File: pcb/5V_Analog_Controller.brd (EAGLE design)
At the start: 50 x 36 mm, 24 parts, among them J1 POWER, Q1 AO3400, Q2 AO3400, U1 ESP32-PICO-MINI-02, U2 AP2112K, X1 PROG, X2 SS-52100-001, X3 SS-52100-001, X5 BOOT, X6 RESET

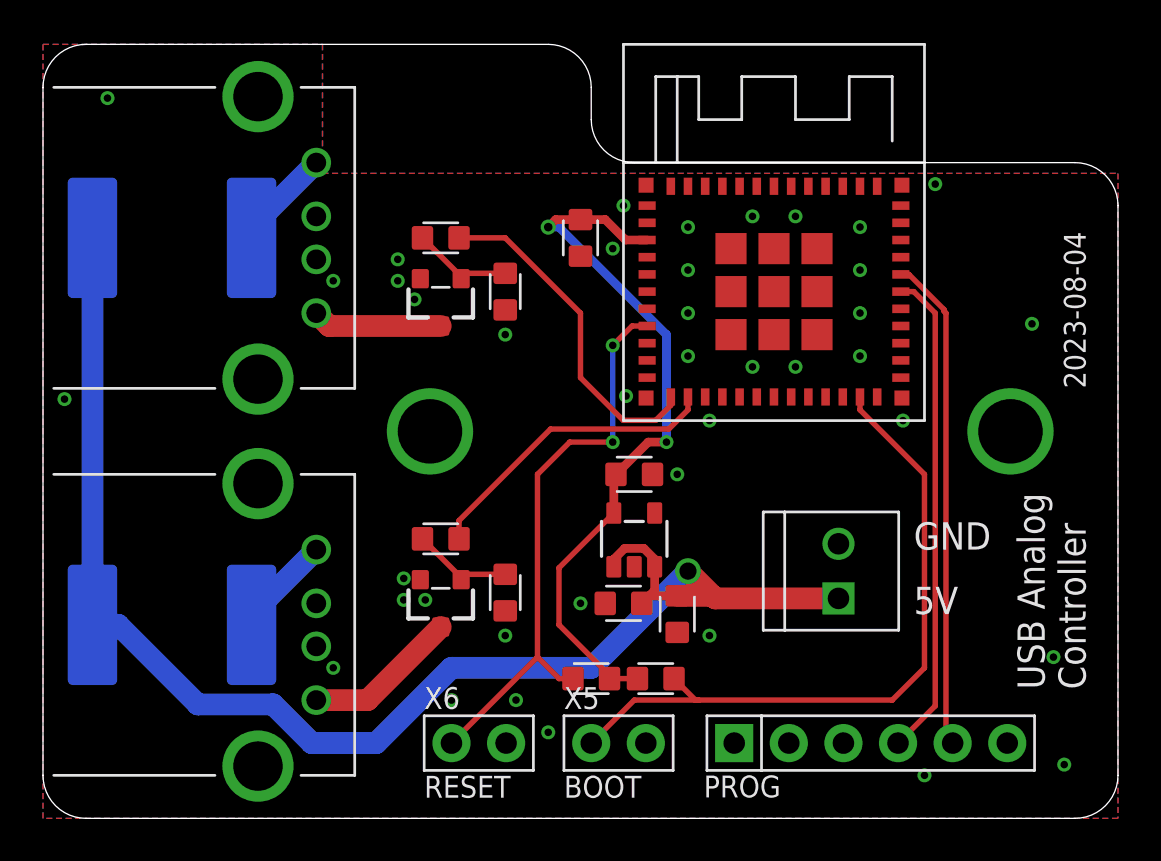
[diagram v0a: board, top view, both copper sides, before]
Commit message: Switch to input power jack
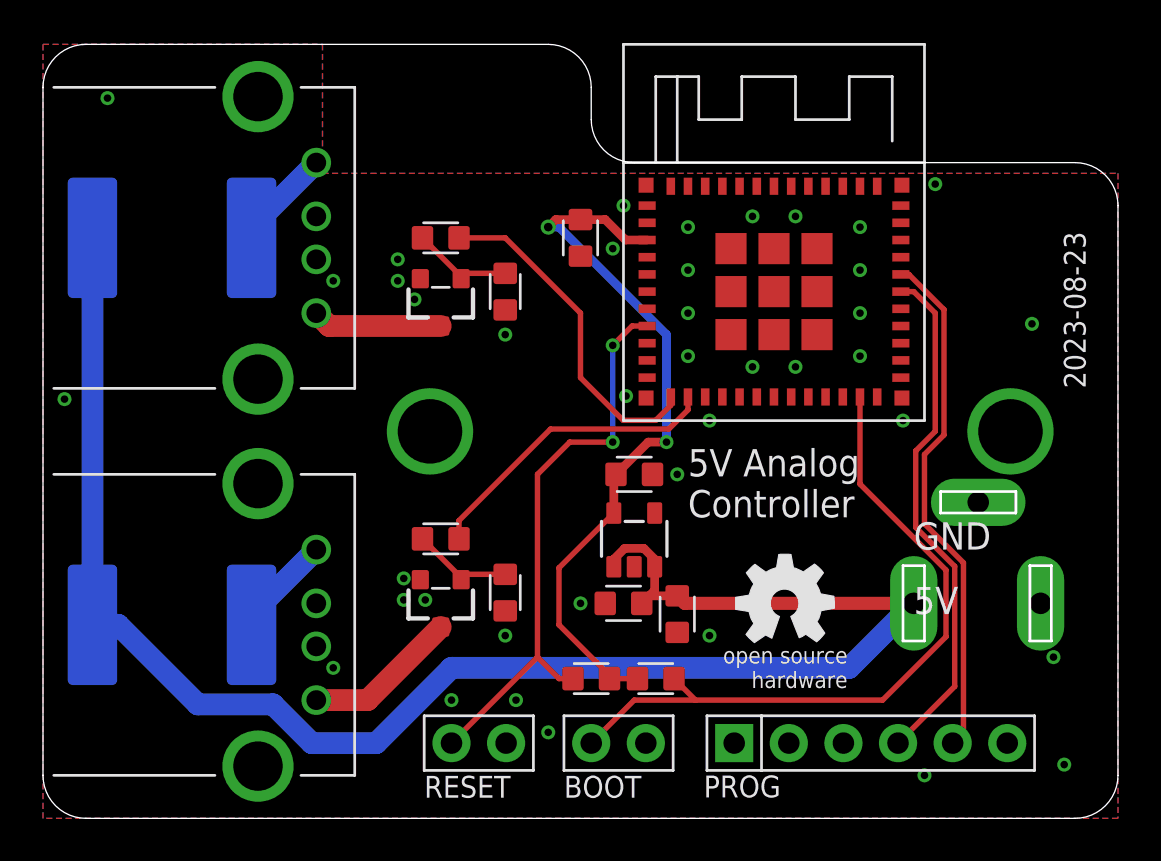
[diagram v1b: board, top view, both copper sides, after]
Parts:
- added U$3: (no value), M2M-Frames:OSHW-5MM-TPLACE
- J1: device M2M-Connectors:TERMINAL-2.54-2P -> M2M-Connectors:XKB-DC-005-5A-2.0
- moved J1 6.67 mm to (43.5, 10.0), turned to 180 degrees
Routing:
- net VIN: track 67.2 -> 79.1 mm, vias 1 -> 0
- net RXD0: track 22.7 -> 24.2 mm
- net TXD0: track 23.0 -> 24.2 mm
- net IO0: track 32.2 -> 32.8 mm
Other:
- board text added: "2023-08-23"
- board text added: "5V Analog Controller"
- board text removed: "2023-08-04"
- board text removed: "USB Analog Controller"
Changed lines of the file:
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@@
 <drawing>
 <settings>
-<setting alwaysvectorfont="no"/>
+<setting alwaysvectorfont="yes"/>
 <setting verticaltext="up"/>
 </settings>
@@
 <wire x1="23.5" y1="36" x2="2" y2="36" width="0" layer="20"/>
 <wire x1="2" y1="36" x2="0" y2="34" width="0" layer="20" curve="90"/>
-<text x="48.5" y="6" size="1.27" layer="21" rot="R90">USB Analog
+<text x="30" y="14" size="1.27" layer="21">5V Analog
 Controller</text>
-<text x="48.5" y="20" size="1.016" layer="21" rot="R90">2023-08-04</text>
+<text x="48.5" y="20" size="1.016" layer="21" rot="R90">2023-08-23</text>
 <text x="40.5" y="12.5" size="1.27" layer="21">GND</text>
 <text x="40.5" y="9.5" size="1.27" layer="21">5V</text>
@@
 <dimension x1="18" y1="18" x2="18" y2="0" x3="-6" y3="9" textsize="1.778" layer="47"/>
 <dimension x1="0" y1="0" x2="0" y2="36" x3="-13" y3="18" textsize="1.778" layer="47"/>
-<text x="54.5" y="20" size="1.778" layer="47">Mounting holes
+<text x="42.5" y="31.5" size="1.778" layer="47">Mounting holes
 2x3mm</text>
 <dimension x1="10" y1="9" x2="10" y2="0" x3="-2.5" y3="4.5" textsize="1.778" layer="47"/>
 <dimension x1="10" y1="27" x2="10" y2="0" x3="-9.5" y3="13.5" textsize="1.778" layer="47"/>
-<dimension x1="48" y1="30.5" x2="48" y2="0" x3="53.5" y3="15.25" textsize="1.778" layer="47"/>
+<dimension x1="48" y1="30.5" x2="48" y2="0" x3="63" y3="15.25" textsize="1.778" layer="47"/>
 <dimension x1="0" y1="34" x2="25.5" y2="34" x3="12.75" y3="38.5" textsize="1.778" layer="47"/>
+<dimension x1="43.5" y1="10" x2="43.5" y2="0" x3="59.5" y3="5" textsize="1.778" layer="47"/>
 </plain>
 <attributes>
@@
 </element>
 <element name="X5" library="M2M-Connectors" package="1X02-2.54" value="BOOT" x="25.5" y="3.5" smashed="yes">
-<attribute name="NAME" x="24.865" y="2.865" size="0.8128" layer="51"/>
 <attribute name="NAME" x="24.23" y="5.0875" size="1.016" layer="25"/>
 <attribute name="NAME" x="24.611" y="2.865" size="1.27" layer="48"/>
+<attribute name="NAME" x="24.865" y="2.865" size="0.8128" layer="51"/>
 <attribute name="VALUE" x="24.23" y="0.96" size="1.016" layer="21"/>
 </element>
 <element name="X6" library="M2M-Connectors" package="1X02-2.54" value="RESET" x="19" y="3.5" smashed="yes">
-<attribute name="NAME" x="18.865" y="2.365" size="0.8128" layer="51"/>
 <attribute name="NAME" x="17.73" y="5.0875" size="1.016" layer="25"/>
 <attribute name="NAME" x="18.111" y="2.865" size="1.27" layer="48"/>
+<attribute name="NAME" x="18.865" y="2.365" size="0.8128" layer="51"/>
 <attribute name="VALUE" x="17.73" y="0.96" size="1.016" layer="21"/>
 </element>
-<element name="J1" library="M2M-Connectors" package="TERMINAL-2.54-2P" value="POWER" x="37" y="11.5" smashed="yes" rot="R90"/>
+<element name="J1" library="M2M-Connectors" package="XKB-DC-005-5A-2.0" value="POWER" x="43.5" y="10" smashed="yes" rot="R180"/>
 <element name="U2" library="M2M-IC" package="SOT23-5" value="AP2112K" x="27.5" y="13" smashed="yes">
 <attribute name="NAME" x="27.495" y="14.805" size="1.016" layer="25" align="bottom-center"/>
@@
 <attribute name="VALUE" x="1" y="13.5" size="1.016" layer="28" rot="MR180"/>
 </element>
+<element name="U$3" library="M2M-Frames" package="OSHW-5MM-TPLACE" value="" x="34.5" y="10" smashed="yes"/>
 </elements>
 <signals>
@@
 <wire x1="26.5" y1="6.5" x2="27.65" y2="6.5" width="0.254" layer="1"/>
 <wire x1="26.55" y1="14.2" x2="24" y2="11.65" width="0.254" layer="1"/>
-<wire x1="24" y1="9" x2="26.5" y2="6.5" width="0.254" layer="1"/>
+<wire x1="24" y1="9" x2="25.75" y2="7.25" width="0.254" layer="1"/>
+<wire x1="25.75" y1="7.25" x2="26.5" y2="6.5" width="0.254" layer="1"/>
 <wire x1="24" y1="11.65" x2="24" y2="9" width="0.254" layer="1"/>
 </signal>
@@
 <contactref element="U1" pad="23"/>
 <contactref element="X5" pad="1"/>
-<wire x1="38" y1="19" x2="38" y2="19.6" width="0.254" layer="1"/>
 <wire x1="25.5" y1="3.5" x2="27.5" y2="5.5" width="0.254" layer="1"/>
-<wire x1="39.5" y1="5.5" x2="41" y2="7" width="0.254" layer="1"/>
-<wire x1="41" y1="7" x2="41" y2="16" width="0.254" layer="1"/>
-<wire x1="41" y1="16" x2="38" y2="19" width="0.254" layer="1"/>
 <wire x1="27.5" y1="5.5" x2="30.35" y2="5.5" width="0.254" layer="1"/>
 <contactref element="R5" pad="1"/>
-<wire x1="30.5" y1="5.5" x2="39.5" y2="5.5" width="0.254" layer="1"/>
 <wire x1="29.35" y1="6.5" x2="30.35" y2="5.5" width="0.254" layer="1"/>
-<wire x1="30.35" y1="5.5" x2="30.5" y2="5.5" width="0.254" layer="1"/>
+<wire x1="30.35" y1="5.5" x2="39.05076875" y2="5.5" width="0.254" layer="1"/>
+<wire x1="39.05076875" y1="5.5" x2="42" y2="8.44923125" width="0.254" layer="1"/>
+<wire x1="42" y1="8.44923125" x2="42" y2="11.55076875" width="0.254" layer="1"/>
+<wire x1="42" y1="11.55076875" x2="38" y2="15.55076875" width="0.254" layer="1"/>
+<wire x1="38" y1="15.55076875" x2="38" y2="19.6" width="0.254" layer="1"/>
 </signal>
 <signal name="EN">
@@
 <contactref element="U1" pad="31"/>
 <contactref element="X1" pad="RX"/>
-<wire x1="41.9064" y1="23.6683375" x2="41.9064" y2="23.5936" width="0.254" layer="1"/>
-<wire x1="41.9064" y1="23.5936" x2="42" y2="23.5" width="0.254" layer="1"/>
-<wire x1="39.9" y1="25.3" x2="40.2747375" y2="25.3" width="0.254" layer="1"/>
-<wire x1="40.2747375" y1="25.3" x2="41.9064" y2="23.6683375" width="0.254" layer="1"/>
-<wire x1="42" y1="3.81" x2="42.31" y2="3.5" width="0.254" layer="1"/>
-<wire x1="42" y1="23.5" x2="42" y2="3.81" width="0.254" layer="1"/>
+<wire x1="39.9" y1="25.3" x2="40" y2="25.3" width="0.254" layer="1"/>
+<wire x1="42.31" y1="3.5" x2="42.8128" y2="4.0028" width="0.254" layer="1"/>
+<wire x1="42.8128" y1="4.0028" x2="42.8128" y2="11.88744375" width="0.254" layer="1"/>
+<wire x1="42.8128" y1="11.88744375" x2="41" y2="13.70024375" width="0.254" layer="1"/>
+<wire x1="41.9064" y1="17.8316625" x2="41.9064" y2="23.6683375" width="0.254" layer="1"/>
+<wire x1="40.2747375" y1="25.3" x2="40" y2="25.3" width="0.254" layer="1"/>
+<wire x1="41" y1="13.70024375" x2="41" y2="16.9252625" width="0.254" layer="1"/>
+<wire x1="41" y1="16.9252625" x2="41.9064" y2="17.8316625" width="0.254" layer="1"/>
+<wire x1="41.9064" y1="23.6683375" x2="40.2747375" y2="25.3" width="0.254" layer="1"/>
 </signal>
 <signal name="RXD0">
 <contactref element="U1" pad="30"/>
 <contactref element="X1" pad="TX"/>
+<wire x1="39.77" y1="3.5" x2="42.4064" y2="6.1364" width="0.254" layer="1"/>
+<wire x1="42.4064" y1="11.71910625" x2="42.4064" y2="6.1364" width="0.254" layer="1"/>
 <wire x1="39.9" y1="24.5" x2="40.5" y2="24.5" width="0.254" layer="1"/>
-<wire x1="41.5" y1="5.23" x2="39.77" y2="3.5" width="0.254" layer="1"/>
+<wire x1="41.5" y1="23.5" x2="41.5" y2="18" width="0.254" layer="1"/>
 <wire x1="40.5" y1="24.5" x2="41.5" y2="23.5" width="0.254" layer="1"/>
-<wire x1="41.5" y1="23.5" x2="41.5" y2="5.23" width="0.254" layer="1"/>
+<wire x1="41.5" y1="18" x2="40.5936" y2="17.0936" width="0.254" layer="1"/>
+<wire x1="40.5936" y1="17.0936" x2="40.5936" y2="13.53190625" width="0.254" layer="1"/>
+<wire x1="40.5936" y1="13.53190625" x2="42.4064" y2="11.71910625" width="0.254" layer="1"/>
 </signal>
 <signal name="N$1">
@@
 <contactref element="U2" pad="3"/>
 <contactref element="C2" pad="1"/>
-<via x="30" y="11.5" extent="1-16" drill="0.8"/>
 <wire x1="28.45" y1="11.7" x2="28.45" y2="10.6" width="0.4064" layer="1"/>
 <wire x1="28.45" y1="10.6" x2="27.85" y2="10" width="0.4064" layer="1"/>
@@
 <wire x1="28.2" y1="10.35" x2="29.5" y2="10.35" width="0.4064" layer="1"/>
 <wire x1="12.5" y1="3.5" x2="15.5" y2="3.5" width="1.016" layer="16"/>
-<wire x1="25.5" y1="7" x2="30" y2="11.5" width="1.016" layer="16"/>
 <wire x1="15.5" y1="3.5" x2="19" y2="7" width="1.016" layer="16"/>
-<wire x1="19" y1="7" x2="25.5" y2="7" width="1.016" layer="16"/>
 <wire x1="26.55" y1="11.7" x2="26.55" y2="12.0516375" width="0.4064" layer="1"/>
 <wire x1="27.0539625" y1="12.5556" x2="26.55" y2="12.0516375" width="0.4064" layer="1"/>
@@
 <wire x1="7.2" y1="5.3" x2="10.7" y2="5.3" width="1.016" layer="16"/>
 <wire x1="3.5" y1="9" x2="7.2" y2="5.3" width="1.016" layer="16"/>
-<wire x1="37" y1="10.23" x2="31.27" y2="10.23" width="1.016" layer="1"/>
-<wire x1="31.15" y1="10.35" x2="30" y2="11.5" width="1.016" layer="1"/>
-<wire x1="29.5" y1="10.35" x2="31.15" y2="10.35" width="1.016" layer="1"/>
-<wire x1="31.15" y1="10.35" x2="31.27" y2="10.23" width="1.016" layer="1"/>
+<wire x1="37.5" y1="7" x2="40.5" y2="10" width="1.016" layer="16"/>
+<wire x1="19" y1="7" x2="37.5" y2="7" width="1.016" layer="16"/>
+<wire x1="40.5" y1="10" x2="29.85" y2="10" width="0.6096" layer="1"/>
+<wire x1="29.85" y1="10" x2="29.5" y2="10.35" width="0.6096" layer="1"/>
 </signal>
 <signal name="N$5">

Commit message: Add reverse power protection for internal circuits
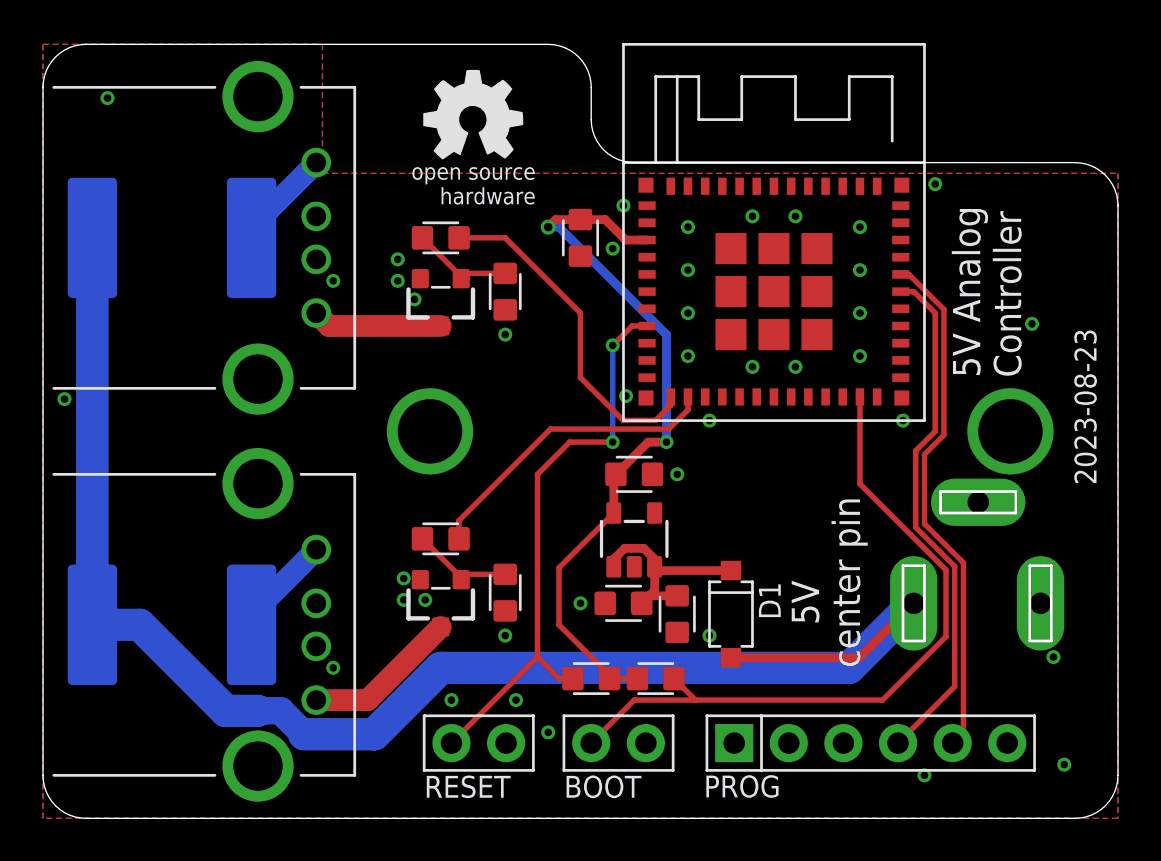
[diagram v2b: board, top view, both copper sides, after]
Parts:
- added D1: B5819LW, M2M-DiscreteSemi:SOD-123
- moved U$3 26.8 mm to (20.0, 32.5)
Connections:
- new net VSW: D1.A, F1.A, F2.A, J1.1
- net VIN: now also D1.C; no longer F1.A, F2.A, J1.1
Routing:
- net VSW: track 0.00 -> 70.4 mm
- net VIN: track 79.1 -> 10.4 mm
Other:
- board text added: "5V center pin"
- board text removed: "5V"
- board text removed: "GND"
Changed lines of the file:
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@@
 <wire x1="23.5" y1="36" x2="2" y2="36" width="0" layer="20"/>
 <wire x1="2" y1="36" x2="0" y2="34" width="0" layer="20" curve="90"/>
-<text x="30" y="14" size="1.27" layer="21">5V Analog
+<text x="45.5" y="20.5" size="1.27" layer="21" rot="R90">5V Analog
 Controller</text>
-<text x="48.5" y="20" size="1.016" layer="21" rot="R90">2023-08-23</text>
-<text x="40.5" y="12.5" size="1.27" layer="21">GND</text>
-<text x="40.5" y="9.5" size="1.27" layer="21">5V</text>
+<text x="49" y="15.5" size="1.016" layer="21" rot="R90">2023-08-23</text>
+<text x="38" y="7" size="1.27" layer="21" rot="R90">    5V
+center pin</text>
 <dimension x1="18" y1="18" x2="0" y2="18" x3="9" y3="-4.5" textsize="1.778" layer="47"/>
 <dimension x1="45" y1="18" x2="0" y2="18" x3="22.5" y3="-8.5" textsize="1.778" layer="47"/>
@@
 <attribute name="VALUE" x="1" y="13.5" size="1.016" layer="28" rot="MR180"/>
 </element>
-<element name="U$3" library="M2M-Frames" package="OSHW-5MM-TPLACE" value="" x="34.5" y="10" smashed="yes"/>
+<element name="U$3" library="M2M-Frames" package="OSHW-5MM-TPLACE" value="" x="20" y="32.5" smashed="yes"/>
+<element name="D1" library="M2M-DiscreteSemi" package="SOD-123" value="B5819LW" x="32" y="9.5" smashed="yes" rot="R270">
+<attribute name="NAME" x="32" y="9.5" size="0.8128" layer="51" rot="R270" align="center"/>
+<attribute name="NAME" x="33.3" y="11" size="1.016" layer="21" rot="R270"/>
+<attribute name="VALUE" x="29.7" y="11" size="1.016" layer="27" rot="R270"/>
+</element>
 </elements>
 <signals>
@@
 <signal name="VIN">
 <contactref element="U2" pad="1"/>
-<contactref element="J1" pad="1"/>
 <contactref element="C3" pad="1"/>
 <contactref element="U2" pad="3"/>
@@
 <wire x1="27.85" y1="10" x2="28.2" y2="10.35" width="0.4064" layer="1"/>
 <wire x1="28.2" y1="10.35" x2="29.5" y2="10.35" width="0.4064" layer="1"/>
-<wire x1="12.5" y1="3.5" x2="15.5" y2="3.5" width="1.016" layer="16"/>
-<wire x1="15.5" y1="3.5" x2="19" y2="7" width="1.016" layer="16"/>
 <wire x1="26.55" y1="11.7" x2="26.55" y2="12.0516375" width="0.4064" layer="1"/>
 <wire x1="27.0539625" y1="12.5556" x2="26.55" y2="12.0516375" width="0.4064" layer="1"/>
@@
 <wire x1="28.45" y1="12.0516375" x2="27.9460375" y2="12.5556" width="0.4064" layer="1"/>
 <wire x1="27.9460375" y1="12.5556" x2="27.0539625" y2="12.5556" width="0.4064" layer="1"/>
-<contactref element="F1" pad="A"/>
-<contactref element="F2" pad="A"/>
-<wire x1="10.7" y1="5.3" x2="12.5" y2="3.5" width="1.016" layer="16"/>
-<wire x1="2.3" y1="27" x2="2.3" y2="9" width="1.016" layer="16"/>
-<wire x1="2.3" y1="9" x2="3.5" y2="9" width="1.016" layer="16"/>
-<wire x1="7.2" y1="5.3" x2="10.7" y2="5.3" width="1.016" layer="16"/>
-<wire x1="3.5" y1="9" x2="7.2" y2="5.3" width="1.016" layer="16"/>
-<wire x1="37.5" y1="7" x2="40.5" y2="10" width="1.016" layer="16"/>
-<wire x1="19" y1="7" x2="37.5" y2="7" width="1.016" layer="16"/>
-<wire x1="40.5" y1="10" x2="29.85" y2="10" width="0.6096" layer="1"/>
-<wire x1="29.85" y1="10" x2="29.5" y2="10.35" width="0.6096" layer="1"/>
+<contactref element="D1" pad="C"/>
+<wire x1="28.45" y1="11.7" x2="28.625" y2="11.525" width="0.4064" layer="1"/>
+<wire x1="28.625" y1="11.525" x2="32" y2="11.525" width="0.4064" layer="1"/>
 </signal>
 <signal name="N$5">
@@
 <wire x1="9.7" y1="9.49" x2="9.7" y2="9" width="1.016" layer="16"/>
 </signal>
+<signal name="VSW">
+<contactref element="F1" pad="A"/>
+<contactref element="F2" pad="A"/>
+<contactref element="J1" pad="1"/>
+<contactref element="D1" pad="A"/>
+<wire x1="32" y1="7.475" x2="37.975" y2="7.475" width="0.4064" layer="1"/>
+<wire x1="37.975" y1="7.475" x2="40.5" y2="10" width="0.4064" layer="1"/>
+<wire x1="2.3" y1="27" x2="2.3" y2="9" width="1.5" layer="16"/>
+<wire x1="40.5" y1="10" x2="37.5" y2="7" width="1.5" layer="16"/>
+<wire x1="37.5" y1="7" x2="18.5" y2="7" width="1.5" layer="16"/>
+<wire x1="18.5" y1="7" x2="15.4076" y2="3.9076" width="1.5" layer="16"/>
+<wire x1="12.14335625" y1="3.9076" x2="15.4076" y2="3.9076" width="1.5" layer="16"/>
+<wire x1="2.3" y1="9" x2="4.5" y2="9" width="1.5" layer="16"/>
+<wire x1="8.5" y1="5" x2="10" y2="5" width="1.5" layer="16"/>
+<wire x1="10" y1="5" x2="11.05095625" y2="5" width="1.27" layer="16"/>
+<wire x1="11.05095625" y1="5" x2="12.14335625" y2="3.9076" width="1.27" layer="16"/>
+<wire x1="4.5" y1="9" x2="8.5" y2="5" width="1.5" layer="16"/>
+</signal>
 </signals>
